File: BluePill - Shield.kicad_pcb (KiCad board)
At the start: 2 copper layers, 40 x 45 mm, 33 parts, among them IC201 ADP2301AUJZ-R7, IC202 ADP2301AUJZ-R7, J201 AMASS_XT30PW-F, J202 AMASS_XT30PW-M, J501 Conn_01x04, J502 Conn_01x02, J504 Conn_01x10, J506 Conn_01x13, U502 TXS0102DCU

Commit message: DRC fix ups
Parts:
- moved C502 3.54 mm to (31.0, 31.8), turned to 0 degrees
- moved J502 2.99 mm to (33.6, 8.50)
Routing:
- net +3V3: track 1.66 -> 17.4 mm, vias 0 -> 2
- net SHIELD_CAN2L: track 26.8 -> 23.8 mm
- net SHIELD_CAN2H: track 26.1 -> 23.2 mm
- net Vdrive: track 59.6 -> 58.6 mm
- net Net-(C207-Pad2): track 31.4 -> 32.4 mm

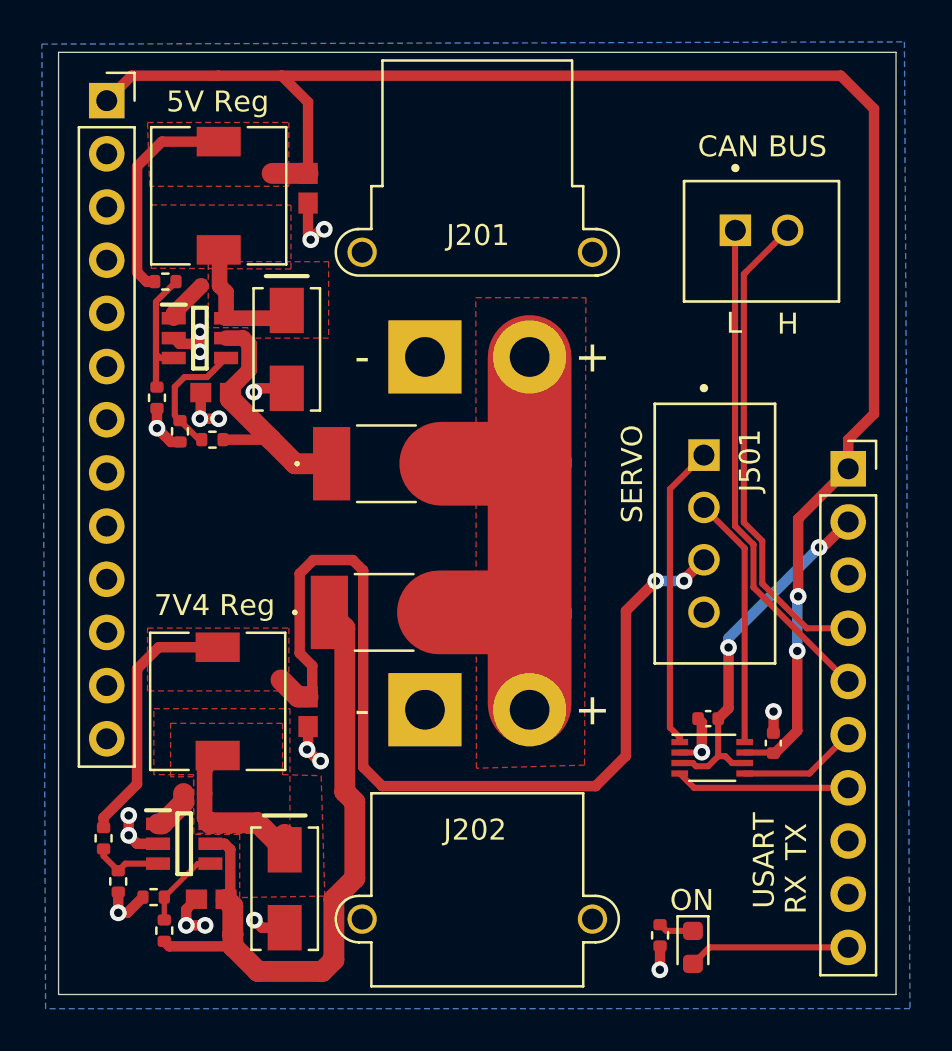
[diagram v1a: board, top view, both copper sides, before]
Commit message: reworked main board for 4 layers
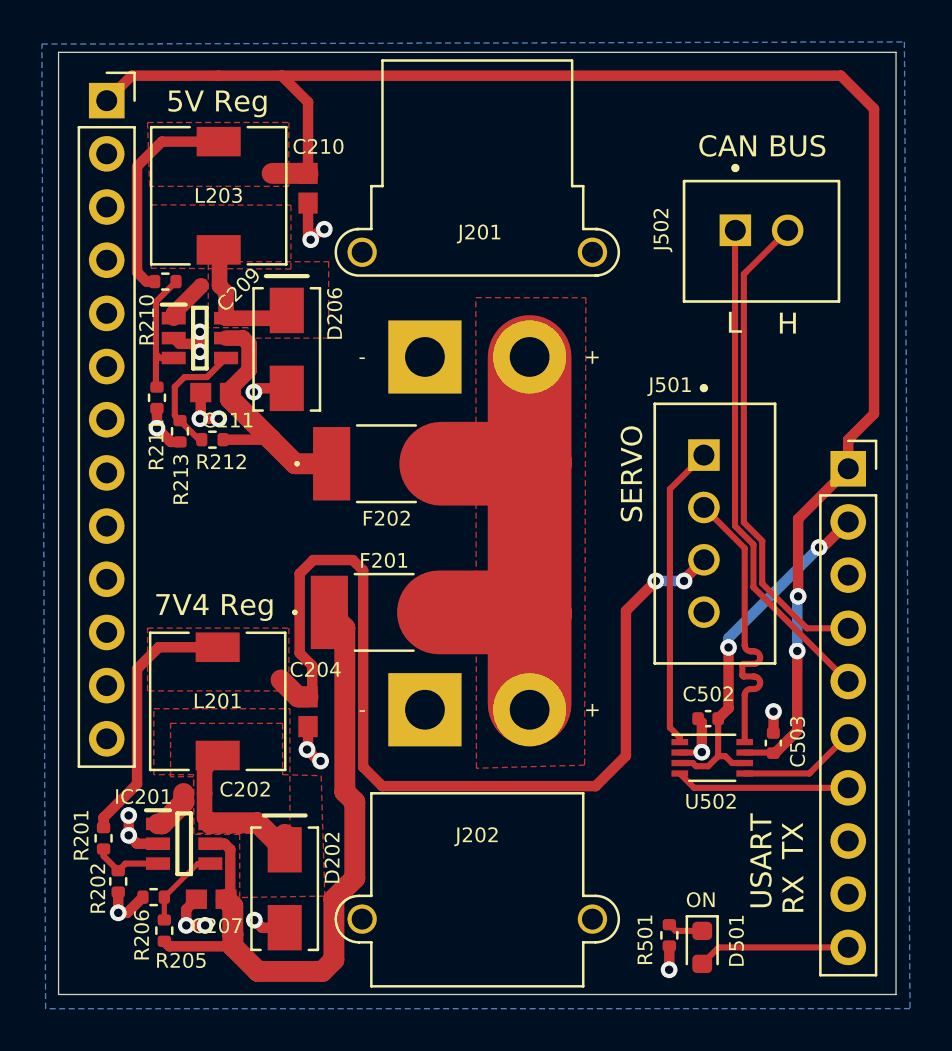
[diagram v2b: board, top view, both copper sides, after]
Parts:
- moved D501 0.44 mm to (30.7, 42.8)
- moved R501 0.44 mm to (29.2, 42.2)
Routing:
- net Servo_TXD: track 12.0 -> 14.3 mm
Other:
- board text added: "Gordon Lay Lui H-P Snek Shield V1.0"

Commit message: ordered
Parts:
- IC201, IC202: footprint BM04B:SOT95P280X100-6N -> SnapEDA Library:SOT95P280X100-6N
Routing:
- net GND: track 27.1 -> 43.3 mm
- net +3V3: track 17.4 -> 20.3 mm
- net Servo_TXD: track 14.3 -> 12.0 mm
- net SHIELD_CAN2L: track 23.8 -> 24.5 mm
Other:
- outline, holes or cut-outs redrawn
- board text added: "IC201"

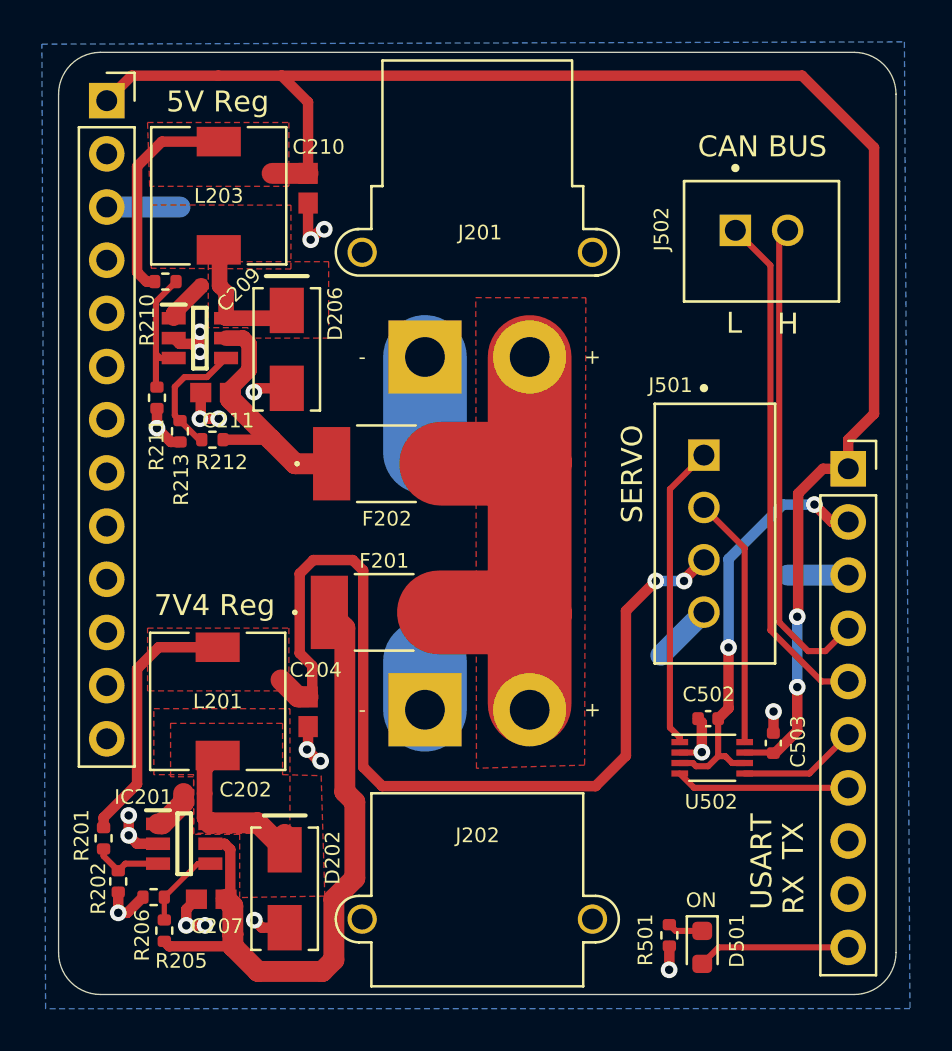
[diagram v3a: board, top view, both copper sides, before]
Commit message: incorporated rework into official design
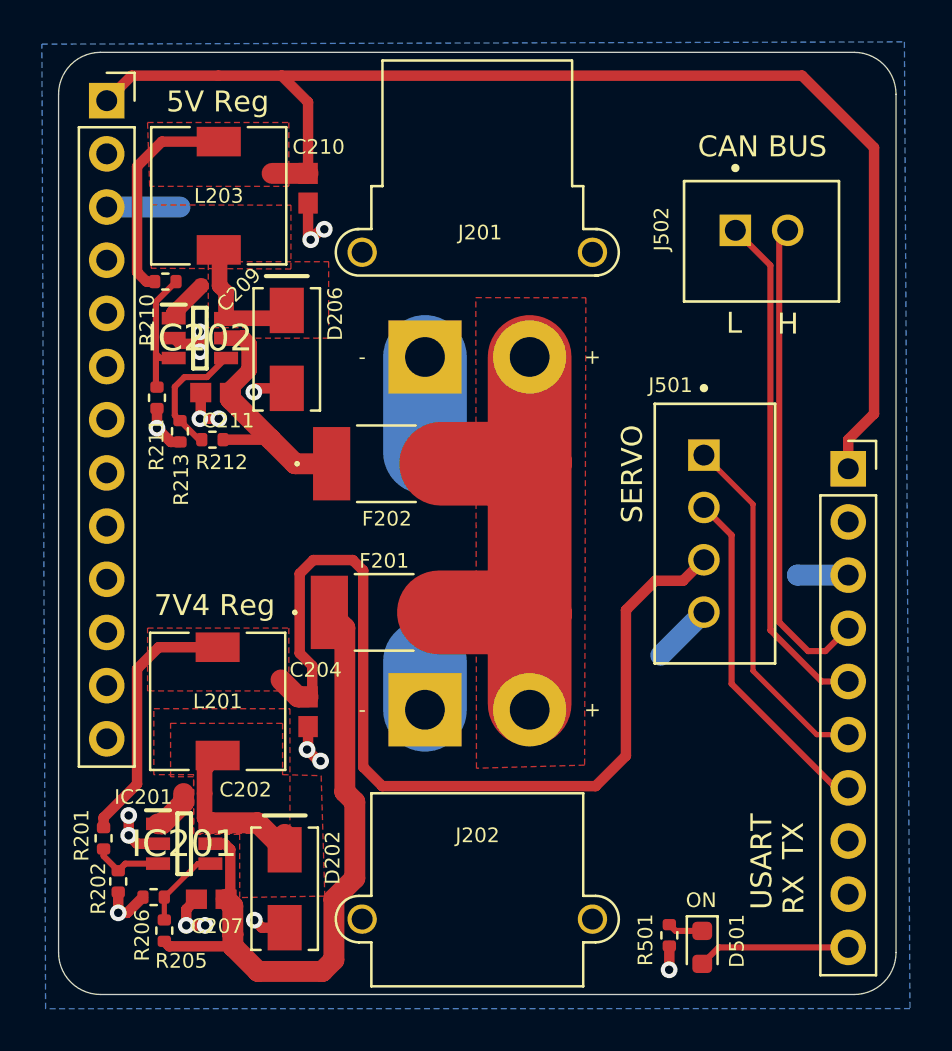
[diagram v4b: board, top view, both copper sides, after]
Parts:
- removed C502, C503: 100n, Capacitor_SMD:C_0402_1005Metric
- removed U502: TXS0102DCU, Package_SO:VSSOP-8_2.3x2mm_P0.5mm
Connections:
- net SHIELD_CAN2H renamed SHIELD_CAN1H
- net SHIELD_CAN2L renamed SHIELD_CAN1L
- J501 pad 1: Servo_RXD -> UART4_TX/SERVO_RX
- J501 pad 2: Servo_TXD -> UART4_RX/SERVO_TX
- J504 pad 6: SHIELD_UART4_TX -> UART4_TX/SERVO_RX
- J504 pad 7: SHIELD_UART4_RX -> UART4_RX/SERVO_TX
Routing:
- net +3V3: track 20.3 -> 0.00 mm, vias 2 -> 0
- net +5V: track 89.0 -> 71.8 mm, vias 2 -> 0
- net UART4_TX/SERVO_RX: track 0.00 -> 17.1 mm
- net UART4_RX/SERVO_TX: track 0.00 -> 16.6 mm
- net Servo_RXD: track 14.6 -> 0.00 mm
- net Servo_TXD: track 12.0 -> 0.00 mm
- net SHIELD_UART4_RX: track 8.33 -> 0.00 mm
- net SHIELD_UART4_TX: track 5.72 -> 0.00 mm
- net GND: track 43.3 -> 39.0 mm, vias 19 -> 17
- net Vdrive: vias 2 -> 0
